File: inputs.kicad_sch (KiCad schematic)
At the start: 82 parts, among them J1 Conn_01x05, J2 Conn_01x05, J3 Conn_01x05, J4 Conn_01x05, J5 Conn_01x05, J6 Conn_01x05, U2 LTV-847S, U3 LTV-847S, U4 LTV-847S, U5 LTV-847S, U6 74HC14, U7 74HC14, U8 74HC14

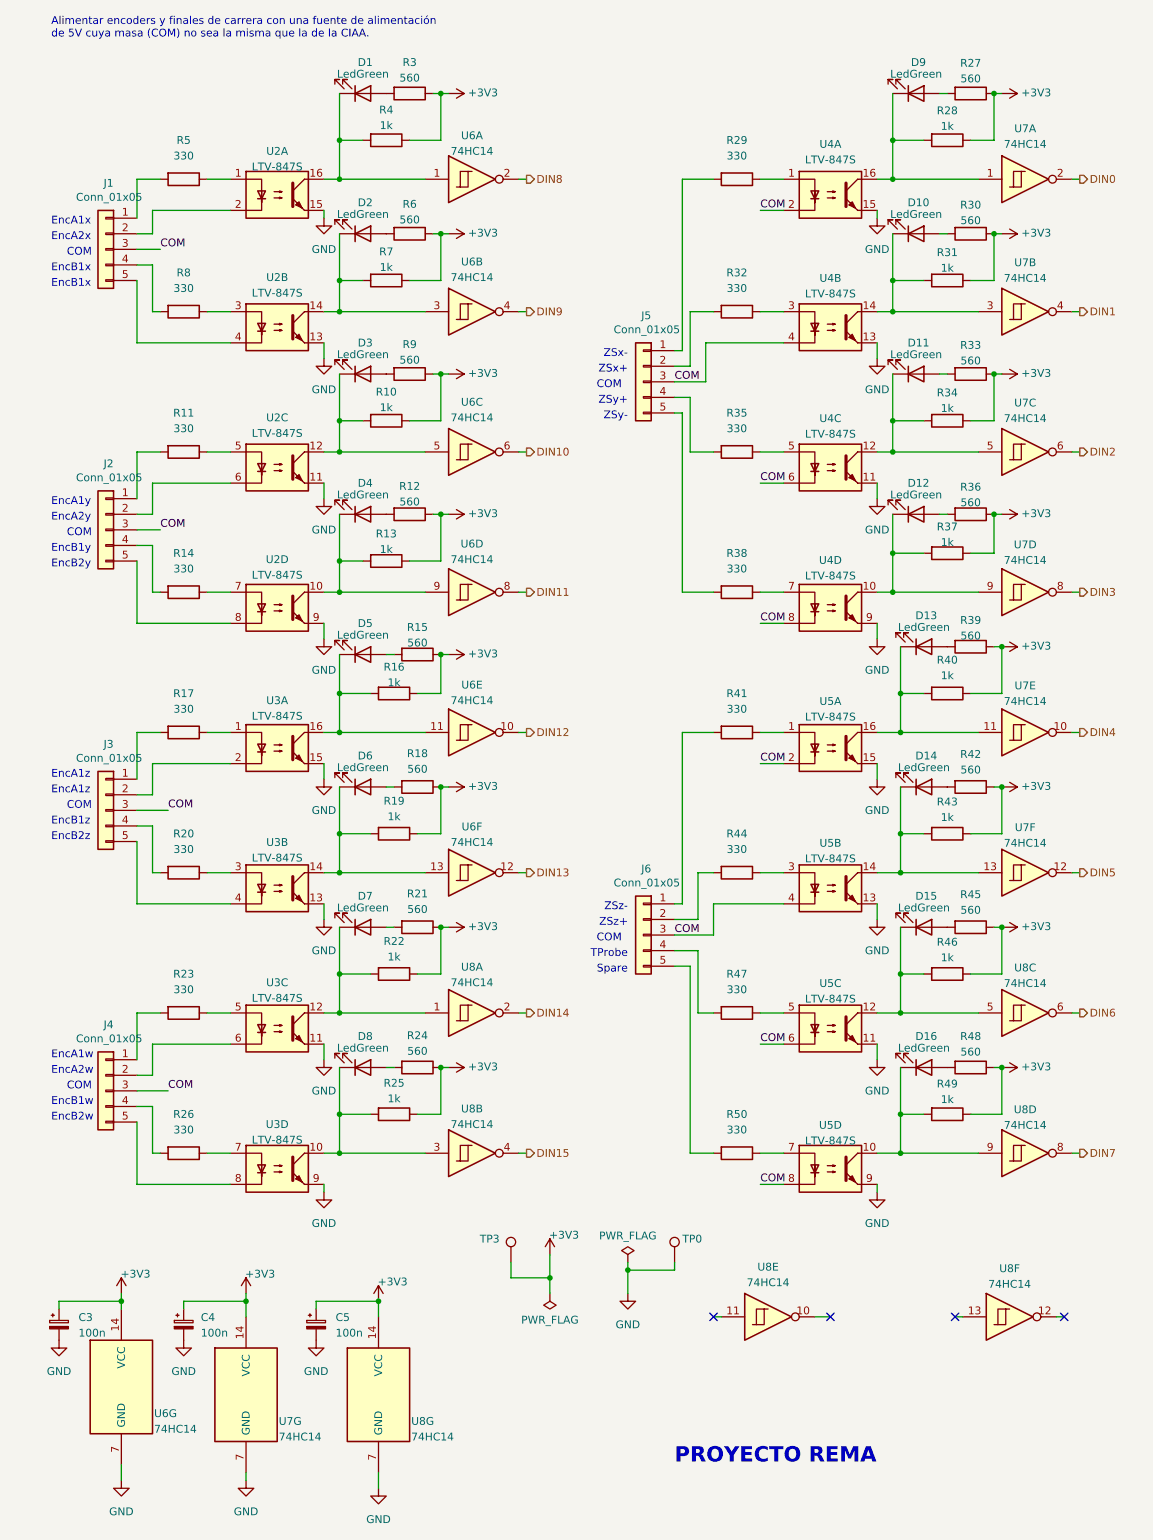
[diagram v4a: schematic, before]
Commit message: Se agregan divisores resisitivos a la salida de los schmitt triggers para asegurar que no le lleguen 5V a las entradas de la pico. Se acutaliza el pcb y se acomodan los componentes en dos capas
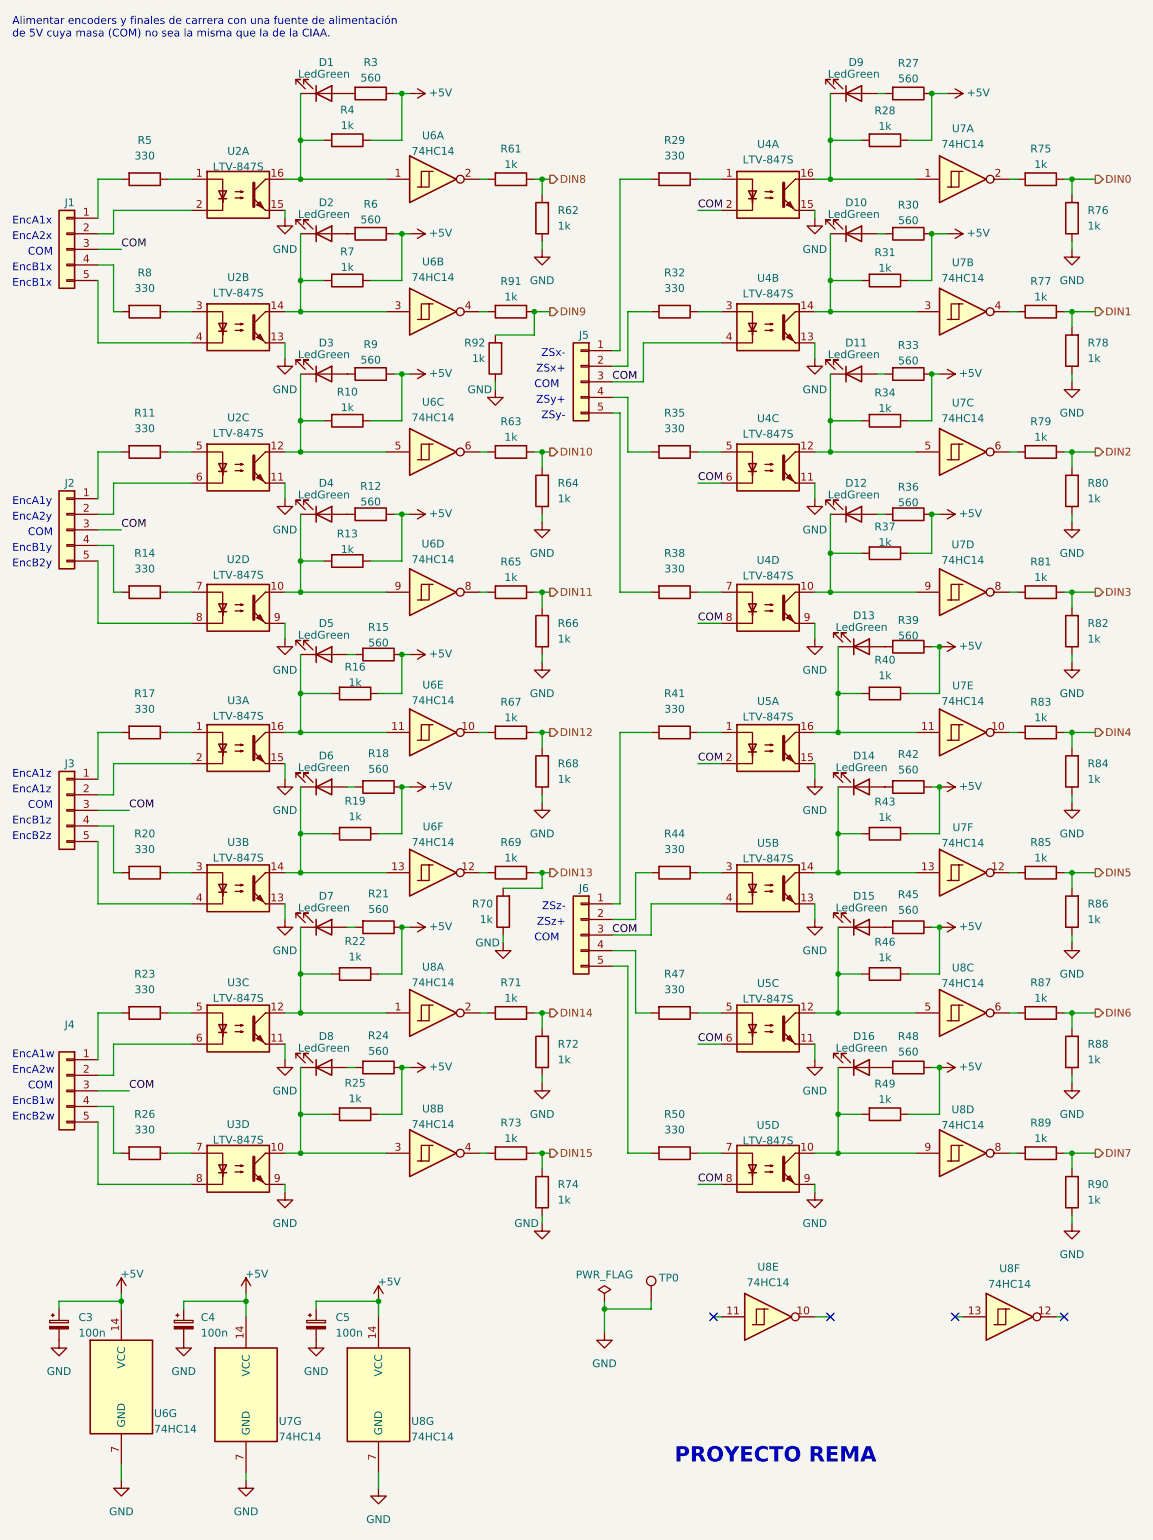
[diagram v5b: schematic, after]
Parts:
- removed TP3: TestPoint, TestPoint:TestPoint_Pad_D2.0mm, symbol Connector:TestPoint
- added R61, R62, R63, R64, R65, R66, R67, R68, R69, R70, R71, R72, R73, R74, R75, R76, R77, R78, R79, R80, R81, R82, R83, R84, R85, R86, R87, R88, R89, R90, R91, R92: 1k, Resistor_SMD:R_1206_3216Metric, symbol Device:R
- U2, U3, U4, U5: footprint Package_DIP:SMDIP-16_W9.53mm -> Package_DIP:DIP-16_W7.62mm_Socket_LongPads
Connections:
- net DIN0: now also R75.1, R76.2; no longer U7.2
- net DIN1: now also R77.1, R78.2; no longer U7.4
- net DIN10: now also R63.1, R64.2; no longer U6.6
- net DIN11: now also R65.1, R66.2; no longer U6.8
- net DIN12: now also R67.1, R68.2; no longer U6.10
- net DIN13: now also R69.1, R70.2; no longer U6.12
- net DIN14: now also R71.1, R72.2; no longer U8.2
- net DIN15: now also R73.1, R74.2; no longer U8.4
- net DIN2: now also R79.1, R80.2; no longer U7.6
- net DIN3: now also R81.1, R82.2; no longer U7.8
- net DIN4: now also R83.1, R84.2; no longer U7.10
- net DIN5: now also R85.1, R86.2; no longer U7.12
- net DIN6: now also R87.1, R88.2; no longer U8.6
- net DIN7: now also R89.1, R90.2; no longer U8.8
- net DIN8: now also R61.1, R62.2; no longer U6.2
- net DIN9: now also R91.1, R92.2; no longer U6.4
- net GND: now also R62.1, R64.1, R66.1, R68.1, R70.1, R72.1, R74.1, R76.1, R78.1, R80.1, R82.1, R84.1, R86.1, R88.1, R90.1, R92.1
- net +3V3 renamed +5V
- new net: R67.2, U6.10
- new net: R73.2, U8.4
- new net: R87.2, U8.6
- new net: R71.2, U8.2
- new net: R85.2, U7.12
- new net: R65.2, U6.8
- new net: R81.2, U7.8
- new net: R89.2, U8.8
- new net: R69.2, U6.12
- new net: R63.2, U6.6
- new net: R83.2, U7.10
- new net: R91.2, U6.4
- new net: R79.2, U7.6
- new net: R61.2, U6.2
- new net: R77.2, U7.4
- new net: R75.2, U7.2
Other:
- note removed: "Spare"
- note removed: "TProbe"
- moved on the sheet: D1, D10, D11, D12, D13, D14, D15, D16, D2, D3, D4, D5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

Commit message: Comienza ruteo en pcb
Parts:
- J1: value Conn_01x05 -> IN_X
- J2: value Conn_01x05 -> IN_Y
- J3: value Conn_01x05 -> IN_Z
- J4: value Conn_01x05 -> IN_W
- J5: value Conn_01x05 -> X_Y_LIMITS
- J6: value Conn_01x05 -> Z_W_LIMITS
- R12, R15, R18, R21, R24, R27, R3, R30, R33, R36, R39, R42, R45, R48, R6, R9: value 560 -> 330
- R61, R63, R65, R67, R69, R71, R73, R75, R77, R79, R81, R83, R85, R87, R89, R91: value 1k -> 100k
- R62, R64, R66, R68, R70, R72, R74, R76, R78, R80, R82, R84, R86, R88, R90: value 1k -> 220k
- renumbered D9 to D0, D10 to D1, D3 to D10, D4 to D11, D5 to D12, D6 to D13, D7 to D14, D8 to D15, D11 to D2, D12 to D3, D13 to D4, D14 to D5, D15 to D6, D16 to D7, D1 to D8, D2 to D9
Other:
- note added: "ZSw+"
- note added: "ZSw-"

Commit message: pcb listo, ver detalles
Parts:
- U2, U3, U4, U5: footprint Package_DIP:DIP-16_W7.62mm_Socket_LongPads -> Package_DIP:DIP-16_W7.62mm_LongPads
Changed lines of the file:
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@@
 			)
 		)
-		(property "Footprint" "Package_DIP:DIP-16_W7.62mm_Socket_LongPads"
+		(property "Footprint" "Package_DIP:DIP-16_W7.62mm_LongPads"
 			(at 137.16 176.53 0)
 			(effects
@@
 			)
 		)
-		(property "Footprint" "Package_DIP:DIP-16_W7.62mm_Socket_LongPads"
+		(property "Footprint" "Package_DIP:DIP-16_W7.62mm_LongPads"
 			(at 50.8 199.39 0)
 			(effects
@@
 			)
 		)
-		(property "Footprint" "Package_DIP:DIP-16_W7.62mm_Socket_LongPads"
+		(property "Footprint" "Package_DIP:DIP-16_W7.62mm_LongPads"
 			(at 50.8 222.25 0)
 			(effects
@@
 			)
 		)
-		(property "Footprint" "Package_DIP:DIP-16_W7.62mm_Socket_LongPads"
+		(property "Footprint" "Package_DIP:DIP-16_W7.62mm_LongPads"
 			(at 50.8 130.81 0)
 			(effects
@@
 			)
 		)
-		(property "Footprint" "Package_DIP:DIP-16_W7.62mm_Socket_LongPads"
+		(property "Footprint" "Package_DIP:DIP-16_W7.62mm_LongPads"
 			(at 50.8 176.53 0)
 			(effects
@@
 			)
 		)
-		(property "Footprint" "Package_DIP:DIP-16_W7.62mm_Socket_LongPads"
+		(property "Footprint" "Package_DIP:DIP-16_W7.62mm_LongPads"
 			(at 137.16 153.67 0)
 			(effects
@@
 			)
 		)
-		(property "Footprint" "Package_DIP:DIP-16_W7.62mm_Socket_LongPads"
+		(property "Footprint" "Package_DIP:DIP-16_W7.62mm_LongPads"
 			(at 137.16 107.95 0)
 			(effects
@@
 			)
 		)
-		(property "Footprint" "Package_DIP:DIP-16_W7.62mm_Socket_LongPads"
+		(property "Footprint" "Package_DIP:DIP-16_W7.62mm_LongPads"
 			(at 50.8 153.67 0)
 			(effects
@@
 			)
 		)
-		(property "Footprint" "Package_DIP:DIP-16_W7.62mm_Socket_LongPads"
+		(property "Footprint" "Package_DIP:DIP-16_W7.62mm_LongPads"
 			(at 137.16 222.25 0)
 			(effects
@@
 			)
 		)
-		(property "Footprint" "Package_DIP:DIP-16_W7.62mm_Socket_LongPads"
+		(property "Footprint" "Package_DIP:DIP-16_W7.62mm_LongPads"
 			(at 50.8 85.09 0)
 			(effects
@@
 			)
 		)
-		(property "Footprint" "Package_DIP:DIP-16_W7.62mm_Socket_LongPads"
+		(property "Footprint" "Package_DIP:DIP-16_W7.62mm_LongPads"
 			(at 137.16 130.81 0)
 			(effects
@@
 			)
 		)
-		(property "Footprint" "Package_DIP:DIP-16_W7.62mm_Socket_LongPads"
+		(property "Footprint" "Package_DIP:DIP-16_W7.62mm_LongPads"
 			(at 50.8 63.5 0)
 			(effects
@@
 			)
 		)
-		(property "Footprint" "Package_DIP:DIP-16_W7.62mm_Socket_LongPads"
+		(property "Footprint" "Package_DIP:DIP-16_W7.62mm_LongPads"
 			(at 137.16 85.09 0)
 			(effects
@@
 			)
 		)
-		(property "Footprint" "Package_DIP:DIP-16_W7.62mm_Socket_LongPads"
+		(property "Footprint" "Package_DIP:DIP-16_W7.62mm_LongPads"
 			(at 137.16 199.39 0)
 			(effects
@@
 			)
 		)
-		(property "Footprint" "Package_DIP:DIP-16_W7.62mm_Socket_LongPads"
+		(property "Footprint" "Package_DIP:DIP-16_W7.62mm_LongPads"
 			(at 137.16 63.5 0)
 			(effects
@@
 			)
 		)
-		(property "Footprint" "Package_DIP:DIP-16_W7.62mm_Socket_LongPads"
+		(property "Footprint" "Package_DIP:DIP-16_W7.62mm_LongPads"
 			(at 50.8 107.95 0)
 			(effects

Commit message: Se generan archivos gerber y se procede a fabricar.
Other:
- note added: "Spare"
- note added: "TProbe"
- note removed: "ZSw+"
- note removed: "ZSw-"
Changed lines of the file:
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@@
 		)
 	)
-	(text "ZSw-"
+	(text "TProbe"
 		(exclude_from_sim no)
 		(at 104.14 180.34 0)
@@
 		)
 	)
-	(text "ZSw+"
+	(text "Spare"
 		(exclude_from_sim no)
 		(at 104.14 182.88 0)
